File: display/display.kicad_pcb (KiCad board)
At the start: 2 copper layers, 68.4 x 20.5 mm, 46 parts, among them P1 CONN_18

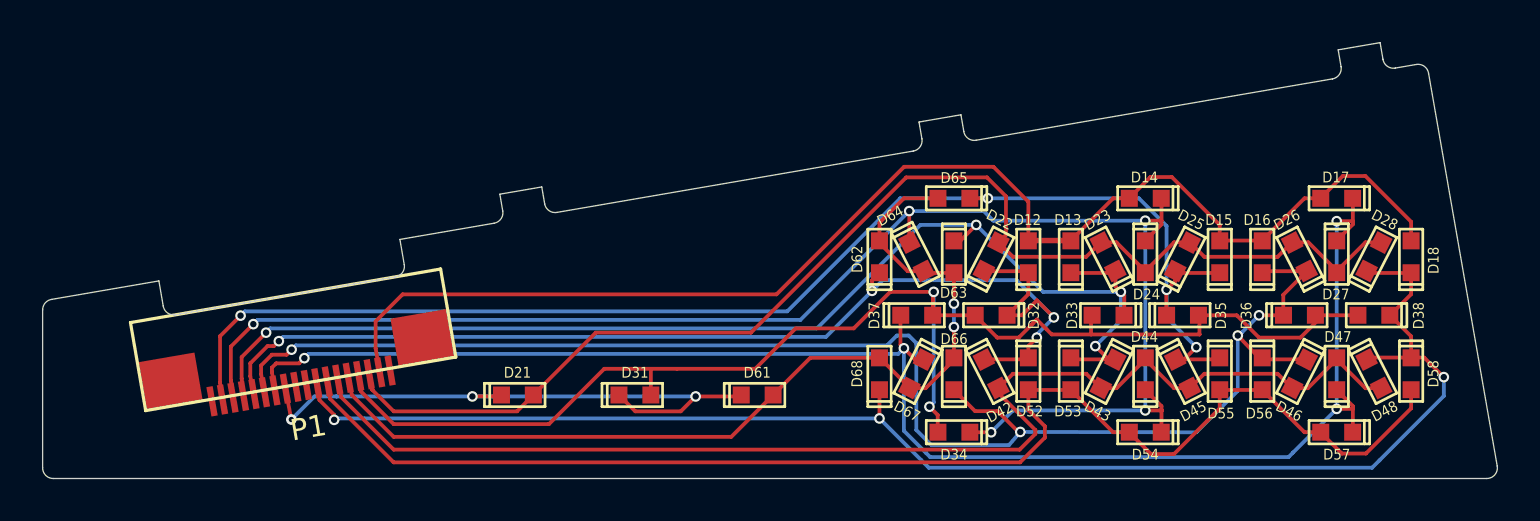
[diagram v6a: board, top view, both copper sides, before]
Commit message: Use 0.5/0.3 mm vias exclusively on the display board.
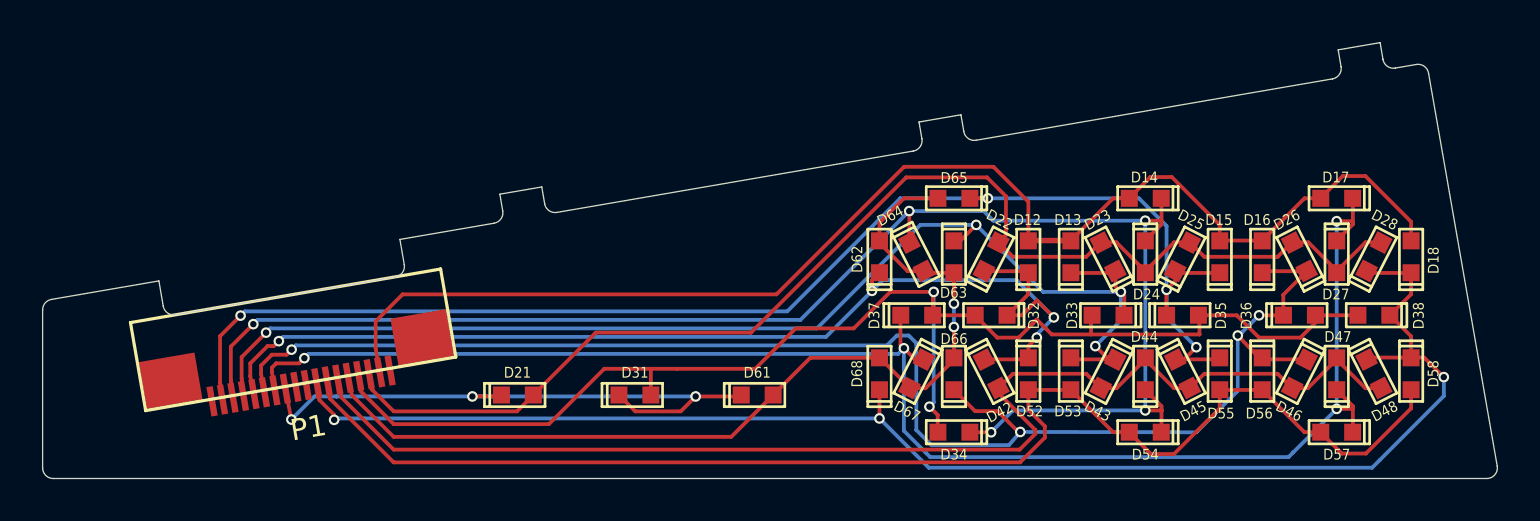
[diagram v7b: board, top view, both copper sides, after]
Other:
- net class Default: via_dia 0.50038 -> 0.5; via_drill 0.29972 -> 0.3
- rule via_min_drill: 0.29972 -> 0.3
- rule via_min_size: 0.50038 -> 0.5

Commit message: Enlarge most of the tracks big time.
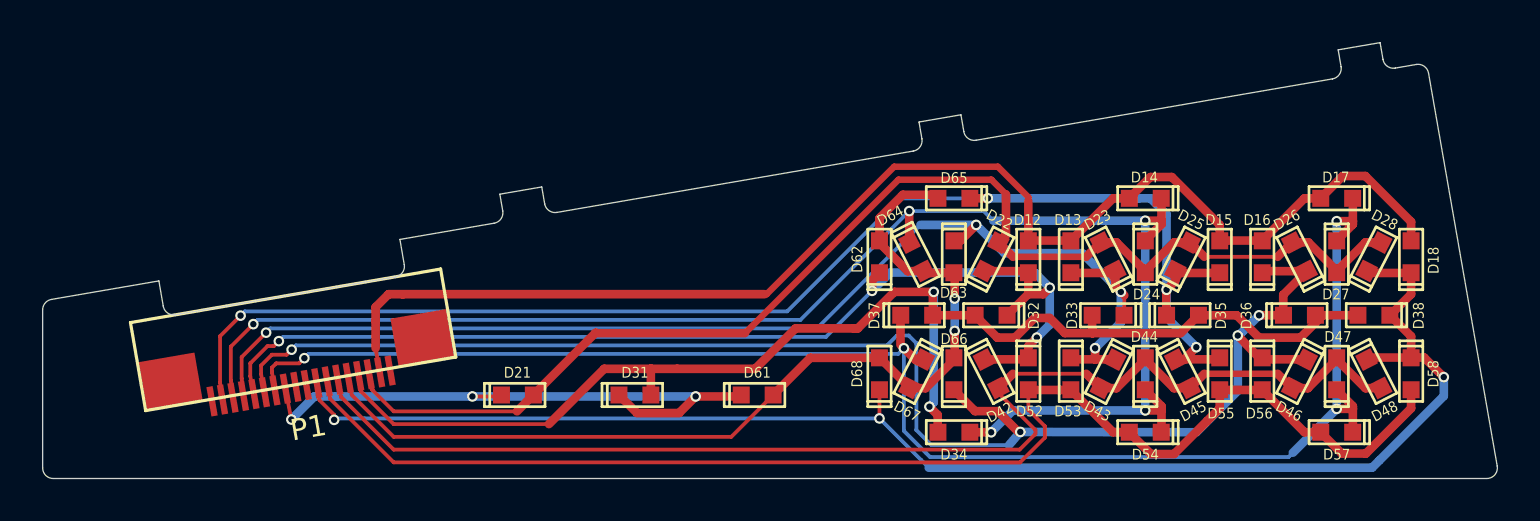
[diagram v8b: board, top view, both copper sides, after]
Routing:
- net /COL2: track 54.4 -> 53.9 mm
- net /ROW1: track 62.6 -> 63.1 mm
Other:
- net class Default: clearance 0.1778 -> 0.2032; trace_width 0.1778 -> 0.2032
- rule trace_clearance: 0.1778 -> 0.2032
- rule trace_min: 0.1778 -> 0.2032
